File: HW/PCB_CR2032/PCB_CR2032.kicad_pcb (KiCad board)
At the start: 2 copper layers, 47.2 x 42 mm, 76 parts, among them J1 DBG, M0 LED, M1 LED, M10 LED, M11 LED, M12 LED, M13 LED, M2 LED, M3 LED, SW1 WAKE, U1 STM32L071CBTx, U3 LIS2DW12, Y1 32768 Hz

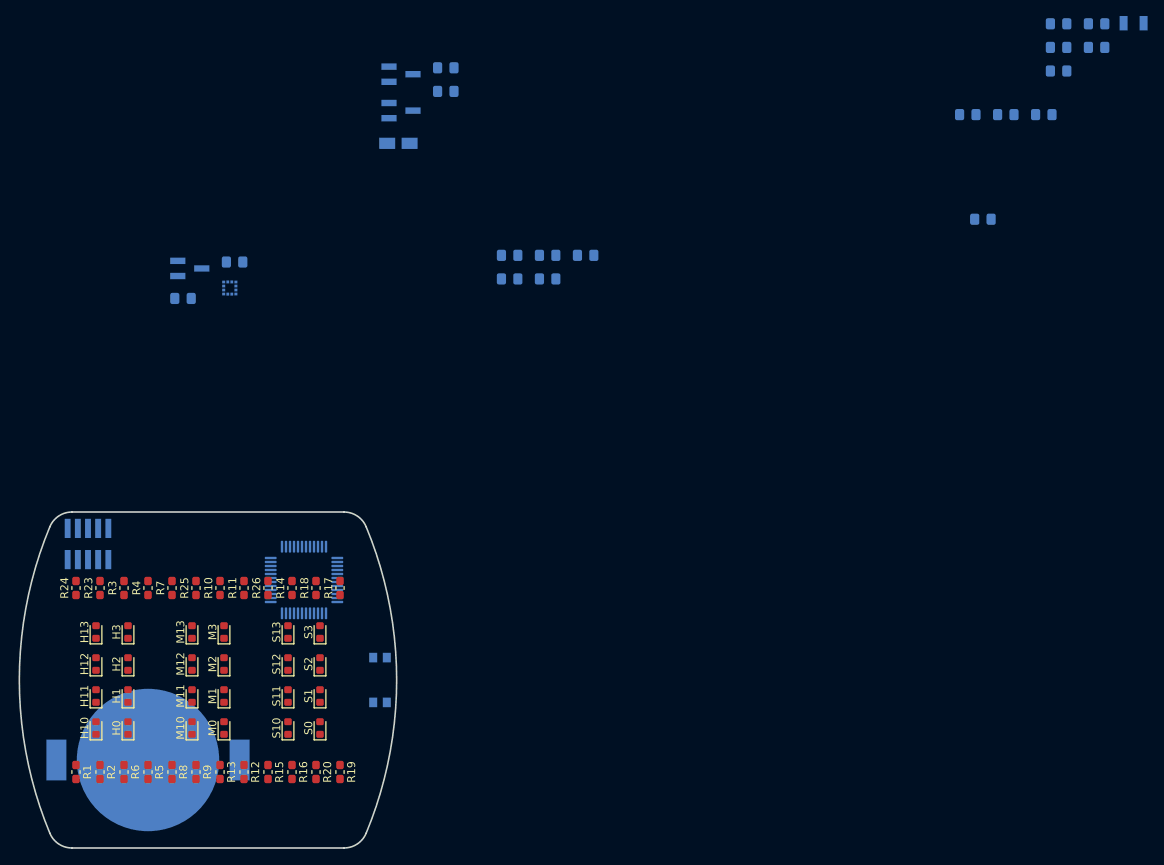
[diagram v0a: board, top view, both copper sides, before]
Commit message: Created layout for CR2032 version 1.0, for first prototype order, resulted in a lot of changes in the pin-mapping to make routing easier.
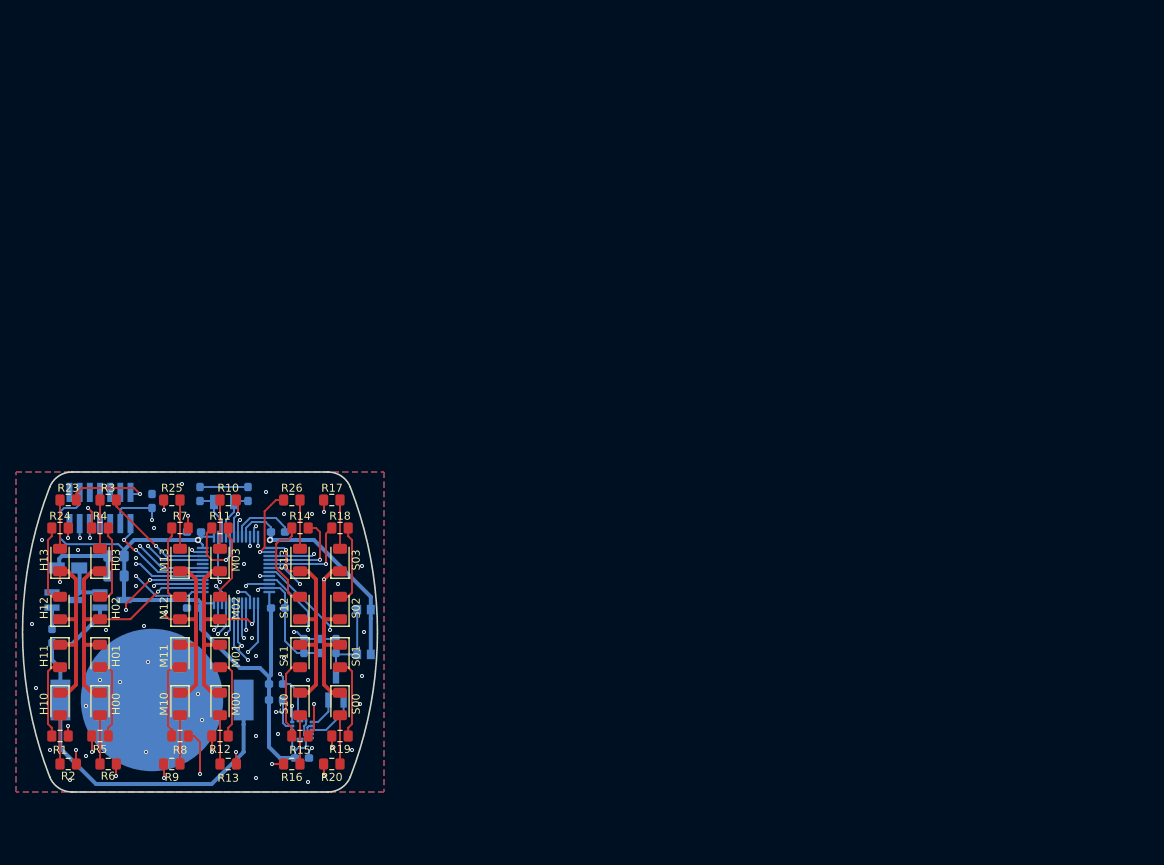
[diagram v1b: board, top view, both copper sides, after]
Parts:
- removed C11: 10uF 10V, Capacitor_SMD:C_0805_2012Metric_Pad1.15x1.40mm_HandSolder
- removed C8: 100nF, Capacitor_SMD:C_0805_2012Metric_Pad1.15x1.40mm_HandSolder
- removed H0, H1, H2, H3, M0, M1, M2, M3, S0, S1, S2, S3: LED, LED_SMD:LED_0603_1608Metric
- removed U3: LIS2DW12, Package_LGA:LGA-12_2x2mm_P0.5mm
- added H00: LED, LED_SMD:LED_1206_3216Metric, F.Cu at (137.5, 109.0)
- added H01: LED, LED_SMD:LED_1206_3216Metric, F.Cu at (137.5, 103.0)
- added H02: LED, LED_SMD:LED_1206_3216Metric, F.Cu at (137.5, 97.0)
- added H03: LED, LED_SMD:LED_1206_3216Metric, F.Cu at (137.5, 91.0)
- added M00: LED, LED_SMD:LED_1206_3216Metric, F.Cu at (152.5, 109.0)
- added M01: LED, LED_SMD:LED_1206_3216Metric, F.Cu at (152.5, 103.0)
- added M02: LED, LED_SMD:LED_1206_3216Metric, F.Cu at (152.5, 97.0)
- added M03: LED, LED_SMD:LED_1206_3216Metric, F.Cu at (152.5, 91.0)
- added S00: LED, LED_SMD:LED_1206_3216Metric, F.Cu at (167.5, 109.0)
- added S01: LED, LED_SMD:LED_1206_3216Metric, F.Cu at (167.5, 103.0)
- added S02: LED, LED_SMD:LED_1206_3216Metric, F.Cu at (167.5, 97.0)
- added S03: LED, LED_SMD:LED_1206_3216Metric, F.Cu at (167.5, 91.0)
- added U2: LIS3DH, Package_LGA:LGA-16_3x3mm_P0.5mm_LayoutBorder3x5y, B.Cu at (162.8, 112.2)
- C1, C2: value 12.5pF -> 20pF; footprint Capacitor_SMD:C_0805_2012Metric_Pad1.15x1.40mm_HandSolder -> Capacitor_SMD:C_0603_1608Metric_Pad1.05x0.95mm_HandSolder
- C13, C3: value 10uF 10V -> 10uF
- C14, C15, C4, C5, C6, C7, C9: footprint Capacitor_SMD:C_0805_2012Metric_Pad1.15x1.40mm_HandSolder -> Capacitor_SMD:C_0603_1608Metric_Pad1.05x0.95mm_HandSolder
- H10, H11, H12, H13, M10, M11, M12, M13, S10, S11, S12, S13: footprint LED_SMD:LED_0603_1608Metric -> LED_SMD:LED_1206_3216Metric
- J1: value DBG -> STDC14; footprint Connector_PinHeader_1.27mm:PinHeader_2x05_P1.27mm_Vertical_SMD -> Connector_PinHeader_1.27mm:PinHeader_2x07_P1.27mm_Vertical_SMD
- R1, R10, R11, R12, R13, R14, R15, R16, R17, R18, R19, R2, R20, R23, R24, R25, R26, R3, R4, R5, R6, R7, R8, R9: value 1.8k -> 1k; footprint Resistor_SMD:R_0603_1608Metric_Pad1.05x0.95mm_HandSolder -> Resistor_SMD:R_0805_2012Metric_Pad1.15x1.40mm_HandSolder
- R27, R28, R29, R30, R31: footprint Resistor_SMD:R_0805_2012Metric_Pad1.15x1.40mm_HandSolder -> Resistor_SMD:R_0603_1608Metric_Pad1.05x0.95mm_HandSolder
- moved C3 132.5 mm to (139.5, 90.5), turned to 180 degrees
- moved Y1 128.5 mm to (153.0, 83.8)
- moved C4 124.0 mm to (159.8, 97.0)
- moved C5 123.9 mm to (149.2, 87.5), turned to 180 degrees
- moved C2 121.3 mm to (156.0, 82.8), turned to 90 degrees
- moved C7 118.7 mm to (149.2, 97.0), turned to 180 degrees
- moved C9 109.7 mm to (144.0, 83.6), turned to 90 degrees
- moved C6 109.0 mm to (159.8, 87.5)
- moved C1 107.1 mm to (150.0, 82.8), turned to 90 degrees
- moved R27 86.4 mm to (131.5, 100.5), turned to 270 degrees
- moved D2 75.0 mm to (139.0, 96.0)
- moved D1 74.3 mm to (133.0, 96.0)
- moved C12 67.3 mm to (133.5, 92.0), turned to 180 degrees
- moved R29 63.4 mm to (159.5, 106.5)
- moved R31 62.8 mm to (159.5, 108.5)
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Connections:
- D2 pad 1: Net-(C12-Pad1) -> Net-(BT1-Pad1)
- D2 pad 2: Net-(BT1-Pad1) -> Net-(C12-Pad1)
- J1 pad 1: VDD -> Net-(J1-Pad1)
- J1 pad 10: /Debug/NRST -> Net-(J1-Pad10)
- J1 pad 2: /Debug/SWDIO -> Net-(J1-Pad2)
- J1 pad 3: GND -> VDD
- J1 pad 4: /Debug/SWCLK -> /Debug/SWDIO
- J1 pad 6: Net-(J1-Pad6) -> /Debug/SWCLK
- J1 pad 7: Net-(J1-Pad7) -> GND
- J1 pad 9: GND -> Net-(J1-Pad9)
- R23 pad 2: /LED/LED_H_13 -> /Debug/DBG_RX
- R24 pad 2: /LED/LED_H_12 -> /Debug/DBG_TX
- U1 pad 10: /LED/LED_H_0_DIM -> /LED/LED_M_12
- U1 pad 11: /LED/LED_H_1_DIM -> /LED/LED_M_13
- U1 pad 12: /LED/LED_M_0_DIM -> /LED/LED_S_0_DIM
- U1 pad 13: /LED/LED_M_1_DIM -> /LED/LED_S_1_DIM
- U1 pad 14: /LED/LED_H_12 -> /LED/LED_S_13
- U1 pad 15: /LED/LED_H_13 -> /LED/LED_S_03
- U1 pad 16: /LED/LED_S_0_DIM -> /LED/LED_S_12
- U1 pad 17: /LED/LED_S_1_DIM -> /LED/LED_S_02
- U1 pad 18: /LED/LED_S_10 -> /LED/LED_S_11
- U1 pad 19: /LED/LED_S_11 -> /LED/LED_S_01
- U1 pad 20: /LED/LED_S_12 -> /LED/LED_S_10
- U1 pad 21: /LED/LED_H_00 -> /LED/LED_S_00
- U1 pad 22: /LED/LED_H_01 -> /LED/LED_M_11
- U1 pad 25: /LED/LED_H_02 -> /LED/LED_M_10
- U1 pad 26: /LED/LED_H_03 -> /LED/LED_M_0_DIM
- U1 pad 27: /LED/LED_H_10 -> /LED/LED_M_1_DIM
- U1 pad 28: /LED/LED_H_11 -> /LED/LED_M_01
- U1 pad 29: /LED/LED_S_00 -> /LED/LED_M_00
- U1 pad 32: /LED/LED_S_01 -> /LED/LED_H_01
- U1 pad 33: /LED/LED_S_02 -> /LED/LED_H_00
- U1 pad 38: /LED/LED_S_03 -> /LED/LED_H_0_DIM
- U1 pad 39: /LED/LED_M_00 -> /LED/LED_H_1_DIM
- U1 pad 40: /LED/LED_M_01 -> /LED/LED_H_10
- U1 pad 41: /LED/LED_M_02 -> /LED/LED_H_11
- U1 pad 42: /LED/LED_M_03 -> /Debug/DBG_TX
- U1 pad 43: /LED/LED_M_10 -> /Debug/DBG_RX
- U1 pad 45: /LED/LED_M_11 -> /LED/LED_H_02
- U1 pad 46: /LED/LED_M_12 -> /LED/LED_H_03
- U1 pad 5: /LED/LED_M_13 -> /LED/LED_M_02
- U1 pad 6: /LED/LED_S_13 -> /LED/LED_M_03
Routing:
- net VDD: track 0.00 -> 132.5 mm, vias 0 -> 2
- net GND: track 0.00 -> 55.3 mm, vias 0 -> 42
- net Net-(BT1-Pad1): track 0.00 -> 55.0 mm
- net /LED/LED_H_1_DIM: track 0.00 -> 42.2 mm, vias 0 -> 2
- net /LED/LED_M_1_DIM: track 0.00 -> 37.1 mm, vias 0 -> 2
- net /LED/LED_H_0_DIM: track 0.00 -> 36.5 mm, vias 0 -> 1
- net /LED/LED_M_11: track 0.00 -> 36.3 mm, vias 0 -> 2
- net /LED/LED_H_11: track 0.00 -> 35.7 mm, vias 0 -> 2
- net /LED/LED_H_10: track 0.00 -> 33.4 mm, vias 0 -> 3
- net /LED/LED_S_0_DIM: track 0.00 -> 33.2 mm, vias 0 -> 2
- net /LED/LED_S_00: track 0.00 -> 29.4 mm, vias 0 -> 2
- net /LED/LED_M_0_DIM: track 0.00 -> 29.0 mm, vias 0 -> 1
- net /LED/LED_H_01: track 0.00 -> 28.9 mm, vias 0 -> 2
- net /LED/LED_H_00: track 0.00 -> 28.8 mm, vias 0 -> 2
- net /LED/LED_M_10: track 0.00 -> 28.5 mm, vias 0 -> 2
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- added copper zone on B.Cu, net GND
- added copper zone on F.Cu, net GND
- added copper zone on In1.Cu, net GND
- added copper zone on In2.Cu, net GND
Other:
- board size 47.2 x 42 mm -> 44.4 x 40 mm
- copper layers 2 -> 4
- net class Default: clearance 0.2 -> 0.15
- rule trace_clearance: 0.2 -> 0.15
- rule via_min_drill: 0.3 -> 0.2
- rule via_min_size: 0.4 -> 0.45

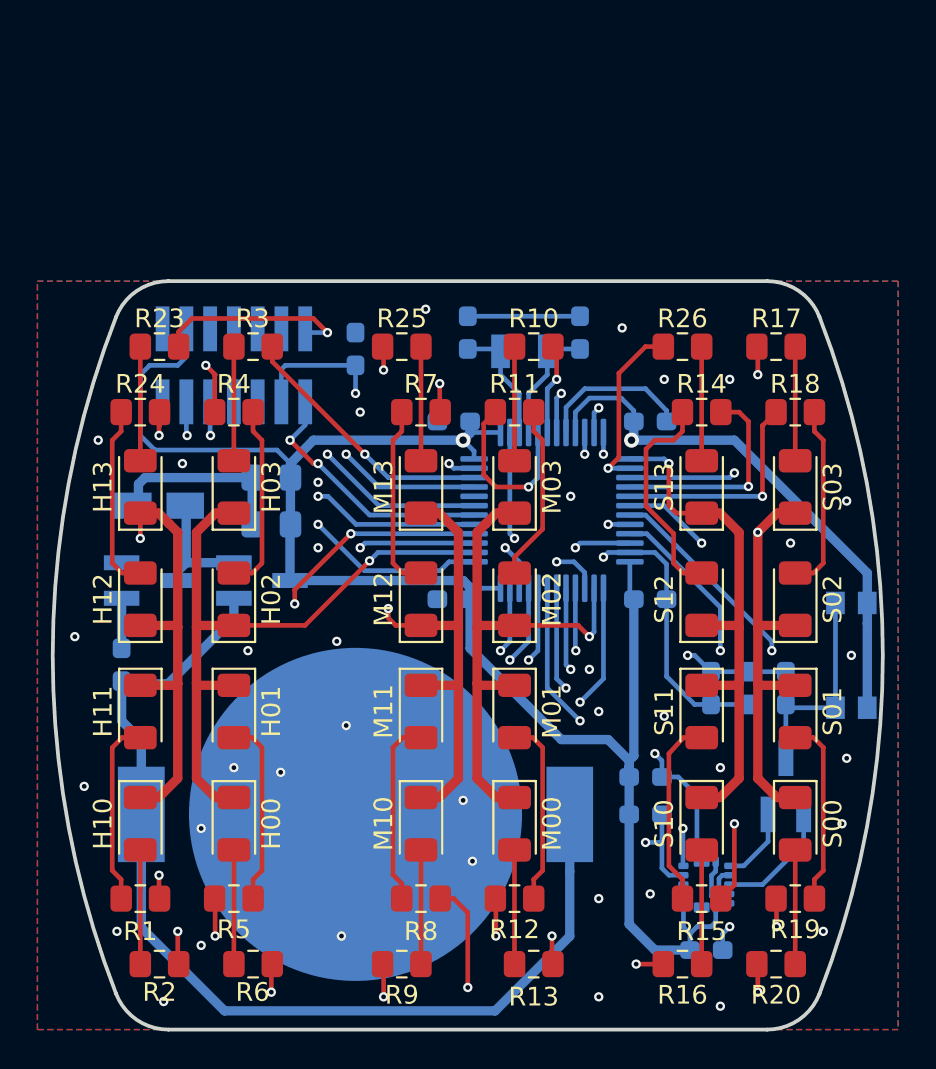
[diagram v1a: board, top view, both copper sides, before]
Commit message: Worked on Rev 2.0 HW with smaller size.
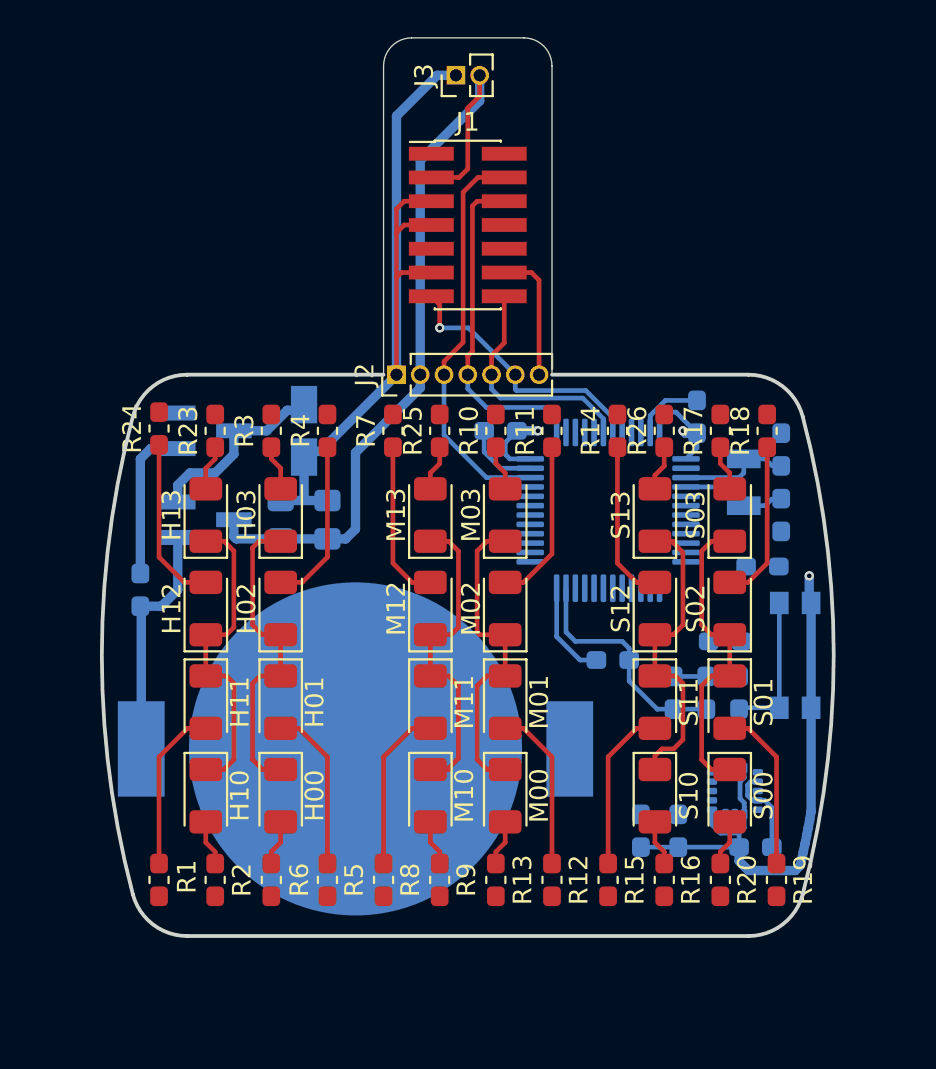
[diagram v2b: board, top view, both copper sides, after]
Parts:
- removed D3: BAR43CFILM, Package_TO_SOT_SMD:SOT-23_Handsoldering
- added J2: Breakoff, Connector_PinHeader_1.27mm:PinHeader_1x07_P1.27mm_Vertical, F.Cu at (146.2, 85.0)
- added J3: PWR, Connector_PinHeader_1.27mm:PinHeader_1x02_P1.27mm_Vertical, F.Cu at (149.4, 69.0)
- J1: moved to F.Cu
- R1, R10, R11, R12, R13, R14, R15, R16, R17, R18, R19, R2, R20, R23, R24, R25, R26, R3, R4, R5, R6, R7, R8, R9: footprint Resistor_SMD:R_0805_2012Metric_Pad1.15x1.40mm_HandSolder -> Resistor_SMD:R_0603_1608Metric_Pad1.05x0.95mm_HandSolder
- R30: value 10k -> 100
- moved C9 25.2 mm to (163.8, 99.2), turned to 0 degrees
- moved C5 18.2 mm to (165.8, 95.2), turned to 0 degrees
- moved C1 17.9 mm to (166.8, 89.0)
- moved J1 14.6 mm to (150.0, 77.0), turned to 0 degrees
- moved C2 14.5 mm to (166.8, 92.5), turned to 270 degrees
- moved Y1 13.7 mm to (164.8, 90.8), turned to 270 degrees
- moved C7 9.34 mm to (151.8, 88.0)
- moved C12 8.72 mm to (141.2, 88.0), turned to 270 degrees
- moved D1 8.54 mm to (136.0, 88.0)
- moved C14 6.09 mm to (165.4, 110.2)
- moved R17 5.39 mm to (163.5, 88.0), turned to 90 degrees
- moved R2 5.39 mm to (136.5, 112.0), turned to 270 degrees
- moved R20 5.39 mm to (163.5, 112.0), turned to 270 degrees
- moved R23 5.39 mm to (136.5, 88.0), turned to 90 degrees
- moved U2 5.23 mm to (164.3, 107.2)
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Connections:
- U2 pad 11: Net-(D3-Pad1) -> /Accelerometer/WAKE_UP
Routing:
- net Net-(BT1-Pad1): track 55.0 -> 12.8 mm
- net /LED/LED_M_11: track 36.3 -> 0.00 mm, vias 2 -> 0
- net /LED/LED_H_11: track 35.7 -> 0.00 mm, vias 2 -> 0
- net /LED/LED_H_10: track 33.4 -> 0.00 mm, vias 3 -> 0
- net /LED/LED_S_00: track 29.4 -> 0.00 mm, vias 2 -> 0
- net /LED/LED_H_01: track 28.9 -> 0.00 mm, vias 2 -> 0
- net /LED/LED_H_00: track 28.8 -> 0.00 mm, vias 2 -> 0
- net /LED/LED_M_10: track 28.5 -> 0.00 mm, vias 2 -> 0
- net /LED/LED_S_01: track 27.2 -> 0.00 mm, vias 2 -> 0
- net /LED/LED_S_10: track 26.7 -> 0.00 mm, vias 2 -> 0
- net /LED/LED_H_1_DIM: track 42.2 -> 17.1 mm, vias 2 -> 0
- net /LED/LED_S_11: track 24.7 -> 0.00 mm, vias 2 -> 0
- net /LED/LED_M_01: track 23.0 -> 0.00 mm, vias 2 -> 0
- net /MCU/ACC_SCL: track 21.7 -> 0.00 mm, vias 2 -> 0
- net VDD: track 132.5 -> 110.9 mm, vias 2 -> 3
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- removed copper zone on B.Cu, net GND
- removed copper zone on F.Cu, net GND
- removed copper zone on In1.Cu, net GND
- removed copper zone on In2.Cu, net GND
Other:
- board size 44.4 x 40 mm -> 39.1 x 48 mm

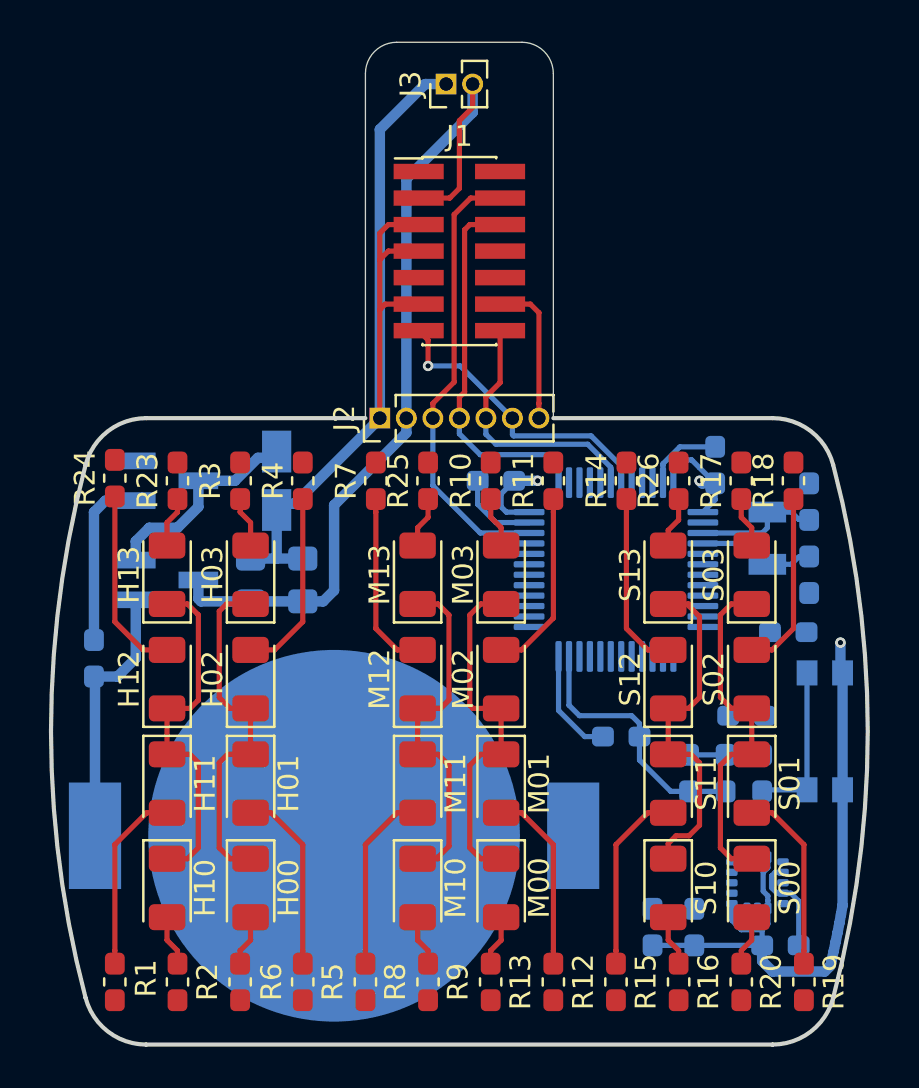
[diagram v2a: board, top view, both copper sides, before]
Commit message: Worked some more on rev 2.0 schematic. Almost done! Also added 3D-model of battery holder to library.
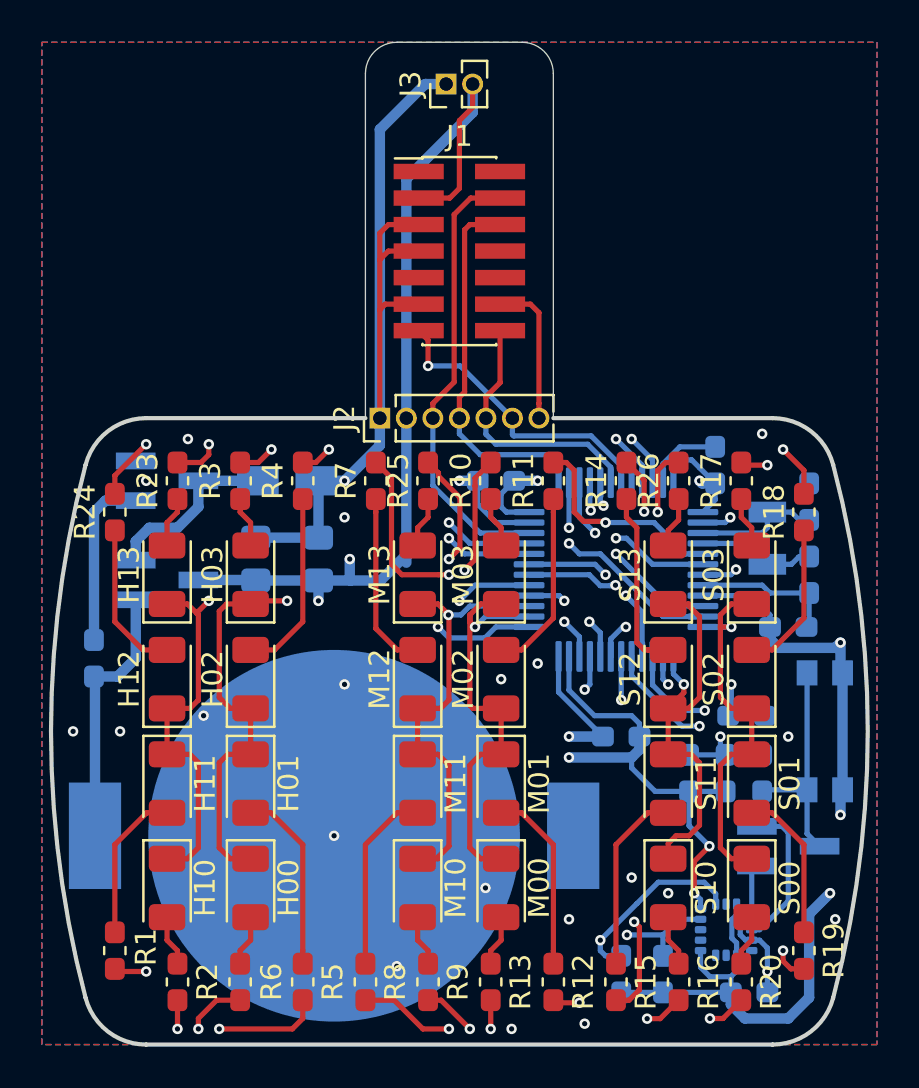
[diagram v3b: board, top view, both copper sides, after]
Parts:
- added D3: BAR43CFILM, Package_TO_SOT_SMD:SOT-23_Handsoldering, B.Cu at (165.8, 105.5)
- moved C14 2.70 mm to (163.9, 112.5)
- moved R29 2.70 mm to (157.8, 111.6)
- moved R31 2.70 mm to (159.8, 111.6)
- moved U2 2.70 mm to (162.8, 109.5)
- moved R24 1.62 mm to (133.5, 89.5)
- moved R18 1.58 mm to (166.5, 89.5)
- moved R1 1.50 mm to (133.5, 110.5)
- moved R19 1.50 mm to (166.5, 110.5)
- moved C13 1.25 mm to (143.2, 91.8)
- moved C3 1.03 mm to (140.2, 91.8)
- moved C12 0.50 mm to (141.8, 88.0), turned to 0 degrees
- moved C5 0.25 mm to (165.8, 95.0)
- turned BT1 to 180 degrees
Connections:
- U2 pad 11: /Accelerometer/WAKE_UP -> Net-(D3-Pad2)
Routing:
- net VDD: track 110.9 -> 151.5 mm, vias 3 -> 8
- net /LED/LED_H_10: track 0.00 -> 39.8 mm, vias 0 -> 2
- net /LED/LED_H_11: track 0.00 -> 39.0 mm, vias 0 -> 2
- net /LED/LED_H_01: track 0.00 -> 37.2 mm, vias 0 -> 2
- net /LED/LED_H_00: track 0.00 -> 36.3 mm, vias 0 -> 2
- net GND: track 69.7 -> 105.1 mm, vias 0 -> 24
- net /LED/LED_M_11: track 0.00 -> 30.5 mm, vias 0 -> 4
- net /MCU/ACC_SDA: track 0.00 -> 30.5 mm, vias 0 -> 2
- net /LED/LED_M_10: track 0.00 -> 27.2 mm, vias 0 -> 2
- net /MCU/ACC_SCL: track 0.00 -> 26.5 mm, vias 0 -> 2
- net /LED/LED_M_00: track 0.00 -> 26.1 mm, vias 0 -> 2
- net /LED/LED_H_1_DIM: track 17.1 -> 41.7 mm, vias 0 -> 2
- net /LED/LED_S_10: track 0.00 -> 23.9 mm, vias 0 -> 2
- net /LED/LED_S_00: track 0.00 -> 23.1 mm, vias 0 -> 2
- net /LED/LED_S_02: track 0.00 -> 23.1 mm, vias 0 -> 2
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- added copper zone on B.Cu, net GND
- added copper zone on F.Cu, net GND
- added copper zone on In1.Cu, net GND
